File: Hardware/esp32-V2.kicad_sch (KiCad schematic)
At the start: 9 parts, among them J11 PM254-1-17-Z-8.5, J13 Conn_01x08, SW4 SW_Push, SW5 SW_Push, U1 ESP32-S31-WROOM-3-N16R16V

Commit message: S31 fully connected
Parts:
- added TP1, TP3, TP4, TP5: TestPoint, TestPoint:TestPoint_Pad_D1.0mm, symbol YV-library:TestPoint
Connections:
- net I34 is gone; now on net IO37: J11.11 (Pin_11)
- net I35 is gone; now on net IO58-UART0-TX: J11.13 (Pin_13)
- net IO0(boot) is gone; now on net IO45: J11.6 (Pin_6)
- net IO21 is gone; now on net IO35: J11.10 (Pin_10)
- net IO22 is gone; now on net IO43: J11.8 (Pin_8)
- net IO25 is gone; now on net IO47: J11.4 (Pin_4)
- net IO26 is gone; now on net IO48: J11.3 (Pin_3)
- net IO27 is gone; now on net IO46: J11.5 (Pin_5)
- net IO32 is gone; now on net IO44: J11.7 (Pin_7)
- net Vbatt-VN is gone; now on net IO59-UART0-RX: J11.12 (Pin_12)
- net CS: now also U1.60 (GPIO50/ADC2_CH0_N)
- net RST: now also U1.59 (GPIO49/ADC1_CH3_P)
- net SCL: now also U1.62 (GPIO52/ADC2_CH1_N)
- net SD0: now also U1.63 (GPIO53/ADC2_CH1_P)
- net SDA: now also U1.61 (GPIO51/ADC2_CH0_P)
- net at U1.40 (USB_DP): now also TP3.1
- net at U1.41 (USB_DM): now also TP4.1
- net IO35: now reaches U1.44 (GPIO35)
- net at U1.45 (GPIO36*): now also TP1.1
- net IO37: now reaches U1.46 (GPIO37)
- net IO43: now reaches U1.53 (GPIO43/ADC1_CH0_P)
- net IO44: now reaches U1.54 (GPIO44/ADC1_CH1_N)
- net IO45: now reaches U1.55 (GPIO45/ADC1_CH1_P)
- net IO46: now reaches U1.56 (GPIO46/ADC1_CH2_N)
- net IO47: now reaches U1.57 (GPIO47/ADC1_CH2_P)
- net IO48: now reaches U1.58 (GPIO48/ADC1_CH3_N)
- net IO58-UART0-TX: now reaches U1.68 (UART0_TXD/GPIO58)
- net IO59-UART0-RX: now reaches U1.69 (UART0_RXD/GPIO59)
- net at U1.70 (GPIO60): now also TP5.1
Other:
- note removed: "I2S_BCLK"
- note removed: "I2S_DOUT"
- note removed: "I2S_LRC"
- note removed: "SCL"
- note removed: "SDA"

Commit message: Schematic Done
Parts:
- removed TP5: TestPoint, TestPoint:TestPoint_Pad_D1.0mm, symbol YV-library:TestPoint
- added R13, R14: 100k, Resistor_SMD:R_0402_1005Metric, symbol Device:R
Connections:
- net +3.3V: now also R13.1, R14.1
- net BOOT: now also R8.2
- net DE: now also U1.49 (GPIO38); no longer U1.25 (GPIO19)
- net DS0: now also U1.10 (GPIO4); no longer U1.6 (GPIO2)
- net DS1: now also U1.11 (GPIO5); no longer U1.7 (GPIO3)
- net DS10: now also U1.17 (GPIO11); no longer U1.13 (GPIO7)
- net DS11: now also U1.18 (GPIO12); no longer U1.14 (GPIO8)
- net DS12: now also U1.19 (GPIO13); no longer U1.15 (GPIO9)
- net DS13: now also U1.20 (GPIO14); no longer U1.16 (GPIO10)
- net DS16: now also U1.21 (GPIO15); no longer U1.17 (GPIO11)
- net DS17: now also U1.22 (GPIO16); no longer U1.18 (GPIO12)
- net DS18: now also U1.23 (GPIO17); no longer U1.19 (GPIO13)
- net DS19: now also U1.24 (GPIO18); no longer U1.20 (GPIO14)
- net DS2: now also U1.12 (GPIO6); no longer U1.8 (GPIO0/XTAL_32K_N)
- net DS20: now also U1.25 (GPIO19); no longer U1.21 (GPIO15)
- net DS3: now also U1.13 (GPIO7); no longer U1.9 (GPIO1/XTAL_32K_P)
- net DS4: now also U1.14 (GPIO8); no longer U1.10 (GPIO4)
- net DS8: now also U1.15 (GPIO9); no longer U1.11 (GPIO5)
- net DS9: now also U1.16 (GPIO10); no longer U1.12 (GPIO6)
- net EN: now also R14.2; no longer R8.2
- net HS: now also U1.51 (GPIO40); no longer U1.23 (GPIO17)
- net I2C1-SCL: now also U1.9 (GPIO1/XTAL_32K_P); no longer U1.49 (GPIO38)
- net I2C1-SDA: now also U1.8 (GPIO0/XTAL_32K_N); no longer U1.50 (GPIO39)
- net IO43: now also J11.3 (Pin_3); no longer J11.8 (Pin_8)
- net IO44: now also J11.4 (Pin_4); no longer J11.7 (Pin_7)
- net IO45: now also J11.5 (Pin_5); no longer J11.6 (Pin_6)
- net IO46: now also J11.6 (Pin_6); no longer J11.5 (Pin_5)
- net IO47: now also J11.7 (Pin_7); no longer J11.4 (Pin_4)
- net IO48: now also J11.8 (Pin_8); no longer J11.3 (Pin_3)
- net IO58-UART0-TX: now also J11.12 (Pin_12); no longer J11.13 (Pin_13)
- net IO59-UART0-RX: now also J11.13 (Pin_13); no longer J11.12 (Pin_12)
- net PCLK: now also U1.52 (GPIO42/ADC1_CH0_N); no longer U1.22 (GPIO16)
- net Touch-INT: now also U1.7 (GPIO3); no longer U1.51 (GPIO40)
- net Touch-RST: now also U1.6 (GPIO2); no longer U1.52 (GPIO42/ADC1_CH0_N)
- net VS: now also U1.50 (GPIO39); no longer U1.24 (GPIO18)
- net BACKLIGHTen: now reaches U1.70 (GPIO60)
- net BACKLIGHTen: now also R13.2
- no-connect marks 10 -> 8
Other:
- note added: "Cristal needed for RTC Wont use it"
- company: (none) -> Motion Composites
- title: ESP32-Power -> Strain Gauge Data Logger
- moved on the sheet: C29, C31, C32, J11, J13, SW4, SW5, TP1, TP3, TP4, U1

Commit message: Layout: unrouted = 0
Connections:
- no-connect marks 8 -> 0
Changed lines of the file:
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@@
 	)
 	(junction
+		(at 92.71 104.14)
+		(diameter 0)
+		(color 0 0 0 0)
+	)
+	(junction
 		(at 259.08 121.92)
 		(diameter 0)
@@
 	)
 	(junction
+		(at 92.71 106.68)
+		(diameter 0)
+		(color 0 0 0 0)
+	)
+	(junction
+		(at 92.71 109.22)
+		(diameter 0)
+		(color 0 0 0 0)
+	)
+	(junction
 		(at 199.39 24.13)
 		(diameter 0)
@@
 	)
 	(junction
+		(at 92.71 116.84)
+		(diameter 0)
+		(color 0 0 0 0)
+	)
+	(junction
 		(at 39.37 187.96)
 		(diameter 0)
@@
 	)
 	(junction
+		(at 92.71 114.3)
+		(diameter 0)
+		(color 0 0 0 0)
+	)
+	(junction
 		(at 102.87 40.64)
 		(diameter 0)
@@
 	)
 	(junction
-		(at 81.28 22.86)
+		(at 92.71 101.6)
 		(diameter 0)
 		(color 0 0 0 0)
 	)
-	(no_connect
-		(at 73.66 109.22)
-	)
-	(no_connect
-		(at 73.66 111.76)
-	)
-	(no_connect
-		(at 73.66 106.68)
-	)
-	(no_connect
-		(at 73.66 114.3)
-	)
-	(no_connect
-		(at 73.66 104.14)
-	)
-	(no_connect
-		(at 73.66 99.06)
-	)
-	(no_connect
-		(at 73.66 101.6)
+	(junction
+		(at 92.71 111.76)
+		(diameter 0)
+		(color 0 0 0 0)
 	)
-	(no_connect
-		(at 73.66 116.84)
+	(junction
+		(at 81.28 22.86)
+		(diameter 0)
+		(color 0 0 0 0)
 	)
 	(bus_entry
@@
 	(wire
 		(pts
+			(xy 92.71 106.68) (xy 92.71 109.22)
+		)
+		(stroke
+			(width 0)
+			(type default)
+		)
+	)
+	(wire
+		(pts
 			(xy 102.87 30.48) (xy 107.95 30.48)
 		)
@@
 	(wire
 		(pts
-			(xy 71.12 116.84) (xy 73.66 116.84)
+			(xy 71.12 116.84) (xy 92.71 116.84)
+		)
+		(stroke
+			(width 0)
+			(type default)
+		)
+	)
+	(wire
+		(pts
+			(xy 92.71 114.3) (xy 92.71 116.84)
 		)
 		(stroke
@@
 	(wire
 		(pts
-			(xy 71.12 106.68) (xy 73.66 106.68)
+			(xy 71.12 106.68) (xy 92.71 106.68)
 		)
 		(stroke
@@
 	(wire
 		(pts
-			(xy 71.12 111.76) (xy 73.66 111.76)
+			(xy 71.12 111.76) (xy 92.71 111.76)
 		)
 		(stroke
@@
 	(wire
 		(pts
+			(xy 92.71 111.76) (xy 92.71 114.3)
+		)
+		(stroke
+			(width 0)
+			(type default)
+		)
+	)
+	(wire
+		(pts
 			(xy 135.89 110.49) (xy 135.89 123.19)
 		)
@@
 	(wire
 		(pts
+			(xy 92.71 109.22) (xy 92.71 111.76)
+		)
+		(stroke
+			(width 0)
+			(type default)
+		)
+	)
+	(wire
+		(pts
 			(xy 194.31 73.66) (xy 213.36 73.66)
 		)
@@
 	(wire
 		(pts
+			(xy 92.71 101.6) (xy 92.71 104.14)
+		)
+		(stroke
+			(width 0)
+			(type default)
+		)
+	)
+	(wire
+		(pts
 			(xy 71.12 66.04) (xy 107.95 66.04)
 		)
@@
 	(wire
 		(pts
-			(xy 71.12 104.14) (xy 73.66 104.14)
+			(xy 71.12 104.14) (xy 92.71 104.14)
 		)
 		(stroke
@@
 	(wire
 		(pts
+			(xy 92.71 104.14) (xy 92.71 106.68)
+		)
+		(stroke
+			(width 0)
+			(type default)
+		)
+	)
+	(wire
+		(pts
 			(xy 97.79 172.72) (xy 104.14 172.72)
 		)
@@
 	(wire
 		(pts
+			(xy 92.71 99.06) (xy 92.71 101.6)
+		)
+		(stroke
+			(width 0)
+			(type default)
+		)
+	)
+	(wire
+		(pts
 			(xy 194.31 78.74) (xy 213.36 78.74)
 		)
@@
 	(wire
 		(pts
+			(xy 92.71 116.84) (xy 92.71 118.11)
+		)
+		(stroke
+			(width 0)
+			(type default)
+		)
+	)
+	(wire
+		(pts
 			(xy 71.12 63.5) (xy 107.95 63.5)
 		)
@@
 	(wire
 		(pts
-			(xy 71.12 101.6) (xy 73.66 101.6)
+			(xy 71.12 101.6) (xy 92.71 101.6)
 		)
 		(stroke
@@
 	(wire
 		(pts
-			(xy 71.12 99.06) (xy 73.66 99.06)
+			(xy 71.12 99.06) (xy 92.71 99.06)
 		)
 		(stroke
@@
 	(wire
 		(pts
-			(xy 71.12 109.22) (xy 73.66 109.22)
+			(xy 71.12 109.22) (xy 92.71 109.22)
 		)
 		(stroke
@@
 	(wire
 		(pts
-			(xy 71.12 114.3) (xy 73.66 114.3)
+			(xy 71.12 114.3) (xy 92.71 114.3)
 		)
 		(stroke
@@
 					(unit 1)
 				)
+			)
+		)
+	)
+	(symbol
+		(lib_id "power:GND")
+		(at 92.71 118.11 0)
+		(unit 1)
+		(body_style 1)
+		(exclude_from_sim no)
+		(in_bom yes)
+		(on_board yes)
+		(in_pos_files yes)
+		(dnp no)
+		(fields_autoplaced yes)
+		(property "Reference" "#PWR012"
+			(at 92.71 124.46 0)
+			(hide yes)
+			(show_name no)
+			(do_not_autoplace no)
+			(effects
+				(font
+					(size 1.27 1.27)
+				)
+			)
+		)
+		(property "Value" "GND"
+			(at 92.71 123.19 0)
+			(hide yes)
+			(show_name no)
+			(do_not_autoplace no)
+			(effects
+				(font
+					(size 1.27 1.27)
+				)
+			)
+		)
+		(property "Footprint" ""
+			(at 92.71 118.11 0)
+			(hide yes)
+			(show_name no)
+			(do_not_autoplace no)
+			(effects
+				(font
+					(size 1.27 1.27)
+				)
+			)
+		)
+		(property "Datasheet" ""
+			(at 92.71 118.11 0)
+			(hide yes)
+			(show_name no)
+			(do_not_autoplace no)
+			(effects
+				(font
+					(size 1.27 1.27)
+				)
+			)
+		)
+		(property "Description" "Power symbol creates a global label with name \"GND\" , ground"
+			(at 92.71 118.11 0)
+			(hide yes)
+			(show_name no)
+			(do_not_autoplace no)
+			(effects
+				(font
+					(size 1.27 1.27)
+				)
+			)
+		)
+		(pin "1"
+		)
+		(instances
+			(project "esp32-V2"
+				(path "/cee18f8d-8618-44b5-96f4-3f3967d85a92/70414f53-588f-4a4a-b5a5-2152d4a63cd4"
+					(reference "#PWR012")
+					(unit 1)
+				)

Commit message: Layout cleaned
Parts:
- renumbered C32 to C33, C31 to C34, C29 to C6, J13 to J3, J11 to J5, R13 to R19, R8 to R30, R14 to R5, SW5 to SW2, SW4 to SW3, TP3 to TP1, TP4 to TP2, TP1 to TP3, U1 to U3
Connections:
- net USB-Dn renamed USB_D-
- net USB-Dp renamed USB_D+
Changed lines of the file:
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@@
+		)
+	)
+	(hierarchical_label "USB_D+"
+		(shape bidirectional)
+		(at 152.4 134.62 180)
+		(effects
+			(font
+				(size 1.524 1.524)
+			)
+			(justify right)
 		)
 	)
@@
 		)
 	)
-	(hierarchical_label "USB-Dn"
+	(hierarchical_label "USB_D-"
 		(shape bidirectional)
 		(at 152.4 132.08 180)
@@
 		(shape output)
 		(at 93.98 55.88 180)
-		(effects
-			(font
-				(size 1.524 1.524)
-			)
-			(justify right)
-		)
-	)
-	(hierarchical_label "USB-Dp"
-		(shape bidirectional)
-		(at 152.4 134.62 180)
 		(effects
 			(font
@@
 		(in_pos_files yes)
 		(dnp no)
-		(property "Reference" "J13"
+		(property "Reference" "J3"
 			(at 108.204 167.386 0)
 			(show_name no)
@@
 			(project "esp32-V2"
 				(path "/cee18f8d-8618-44b5-96f4-3f3967d85a92/70414f53-588f-4a4a-b5a5-2152d4a63cd4"
-					(reference "J13")
+					(reference "J3")
 					(unit 1)
 				)
@@
 		(in_pos_files yes)
 		(dnp no)
-		(property "Reference" "SW4"
+		(property "Reference" "SW3"
 			(at 266.7 116.586 0)
 			(show_name no)
@@
 			(project "esp32-V2"
 				(path "/cee18f8d-8618-44b5-96f4-3f3967d85a92/70414f53-588f-4a4a-b5a5-2152d4a63cd4"
-					(reference "SW4")
+					(reference "SW3")
 					(unit 1)
 				)
@@
 		(dnp no)
 		(fields_autoplaced yes)
-		(property "Reference" "U1"
+		(property "Reference" "U3"
 			(at 151.13 21.59 0)
 			(show_name no)
@@
 			(project "esp32-V2"
 				(path "/cee18f8d-8618-44b5-96f4-3f3967d85a92/70414f53-588f-4a4a-b5a5-2152d4a63cd4"
-					(reference "U1")
+					(reference "U3")
 					(unit 1)
 				)
@@
 		(in_pos_files yes)
 		(dnp no)
-		(property "Reference" "R13"
+		(property "Reference" "R19"
 			(at 205.74 27.9399 0)
 			(show_name no)
@@
 			(project "esp32-V2"
 				(path "/cee18f8d-8618-44b5-96f4-3f3967d85a92/70414f53-588f-4a4a-b5a5-2152d4a63cd4"
-					(reference "R13")
+					(reference "R19")
 					(unit 1)
 				)
@@
 		(in_pos_files yes)
 		(dnp no)
-		(property "Reference" "SW5"
+		(property "Reference" "SW2"
 			(at 267.716 143.51 0)
 			(show_name no)
@@
 			(project "esp32-V2"
 				(path "/cee18f8d-8618-44b5-96f4-3f3967d85a92/70414f53-588f-4a4a-b5a5-2152d4a63cd4"
-					(reference "SW5")
+					(reference "SW2")
 					(unit 1)
 				)
@@
 		(in_pos_files yes)
 		(dnp no)
-		(property "Reference" "C32"
+		(property "Reference" "C33"
 			(at 258.064 151.384 0)
 			(show_name no)
@@
 			(project "esp32-V2"
 				(path "/cee18f8d-8618-44b5-96f4-3f3967d85a92/70414f53-588f-4a4a-b5a5-2152d4a63cd4"
-					(reference "C32")
+					(reference "C33")
 					(unit 1)
 				)
@@
 		(in_pos_files yes)
 		(dnp no)
-		(property "Reference" "J11"
+		(property "Reference" "J5"
 			(at 29.464 144.526 0)
 			(show_name no)
@@
 			(project "esp32-V2"
 				(path "/cee18f8d-8618-44b5-96f4-3f3967d85a92/70414f53-588f-4a4a-b5a5-2152d4a63cd4"
-					(reference "J11")
+					(reference "J5")
 					(unit 1)
 				)
@@
 		(in_pos_files yes)
 		(dnp no)
-		(property "Reference" "TP3"
+		(property "Reference" "TP1"
 			(at 151.13 127.508 90)
 			(show_name no)
@@
 			(project "esp32-V2"
 				(path "/cee18f8d-8618-44b5-96f4-3f3967d85a92/70414f53-588f-4a4a-b5a5-2152d4a63cd4"
-					(reference "TP3")
+					(reference "TP1")
 					(unit 1)
 				)
@@
 		(in_pos_files yes)
 		(dnp no)
-		(property "Reference" "TP4"
+		(property "Reference" "TP2"
 			(at 153.67 127.508 90)
 			(show_name no)
@@
 			(project "esp32-V2"
 				(path "/cee18f8d-8618-44b5-96f4-3f3967d85a92/70414f53-588f-4a4a-b5a5-2152d4a63cd4"
-					(reference "TP4")
+					(reference "TP2")
 					(unit 1)
 				)
@@
 		(in_pos_files yes)
 		(dnp no)
-		(property "Reference" "C31"
+		(property "Reference" "C34"
 			(at 260.604 124.714 0)
 			(show_name no)
@@
 			(project "esp32-V2"
 				(path "/cee18f8d-8618-44b5-96f4-3f3967d85a92/70414f53-588f-4a4a-b5a5-2152d4a63cd4"
-					(reference "C31")
+					(reference "C34")
 					(unit 1)
 				)
@@
 		(in_pos_files yes)
 		(dnp no)
-		(property "Reference" "R14"
+		(property "Reference" "R5"
 			(at 97.536 36.83 0)
 			(show_name no)
@@
 			(project "esp32-V2"
 				(path "/cee18f8d-8618-44b5-96f4-3f3967d85a92/70414f53-588f-4a4a-b5a5-2152d4a63cd4"
-					(reference "R14")
+					(reference "R5")
 					(unit 1)
 				)
@@
 		(in_pos_files yes)
 		(dnp no)
-		(property "Reference" "TP1"
+		(property "Reference" "TP3"
 			(at 163.83 127.508 90)
 			(show_name no)
@@
 			(project "esp32-V2"
 				(path "/cee18f8d-8618-44b5-96f4-3f3967d85a92/70414f53-588f-4a4a-b5a5-2152d4a63cd4"
-					(reference "TP1")
+					(reference "TP3")
 					(unit 1)
 				)
@@
 		(in_pos_files yes)
 		(dnp no)
-		(property "Reference" "C29"
+		(property "Reference" "C6"
 			(at 82.804 25.654 0)
 			(show_name no)
@@
 			(project "esp32-V2"
 				(path "/cee18f8d-8618-44b5-96f4-3f3967d85a92/70414f53-588f-4a4a-b5a5-2152d4a63cd4"
-					(reference "C29")
+					(reference "C6")
 					(unit 1)
 				)
@@
 		(in_pos_files yes)
 		(dnp no)
-		(property "Reference" "R8"
+		(property "Reference" "R30"
 			(at 195.326 27.686 0)
 			(show_name no)
@@
 			(project "esp32-V2"
 				(path "/cee18f8d-8618-44b5-96f4-3f3967d85a92/70414f53-588f-4a4a-b5a5-2152d4a63cd4"
-					(reference "R8")
+					(reference "R30")
 					(unit 1)
 				)

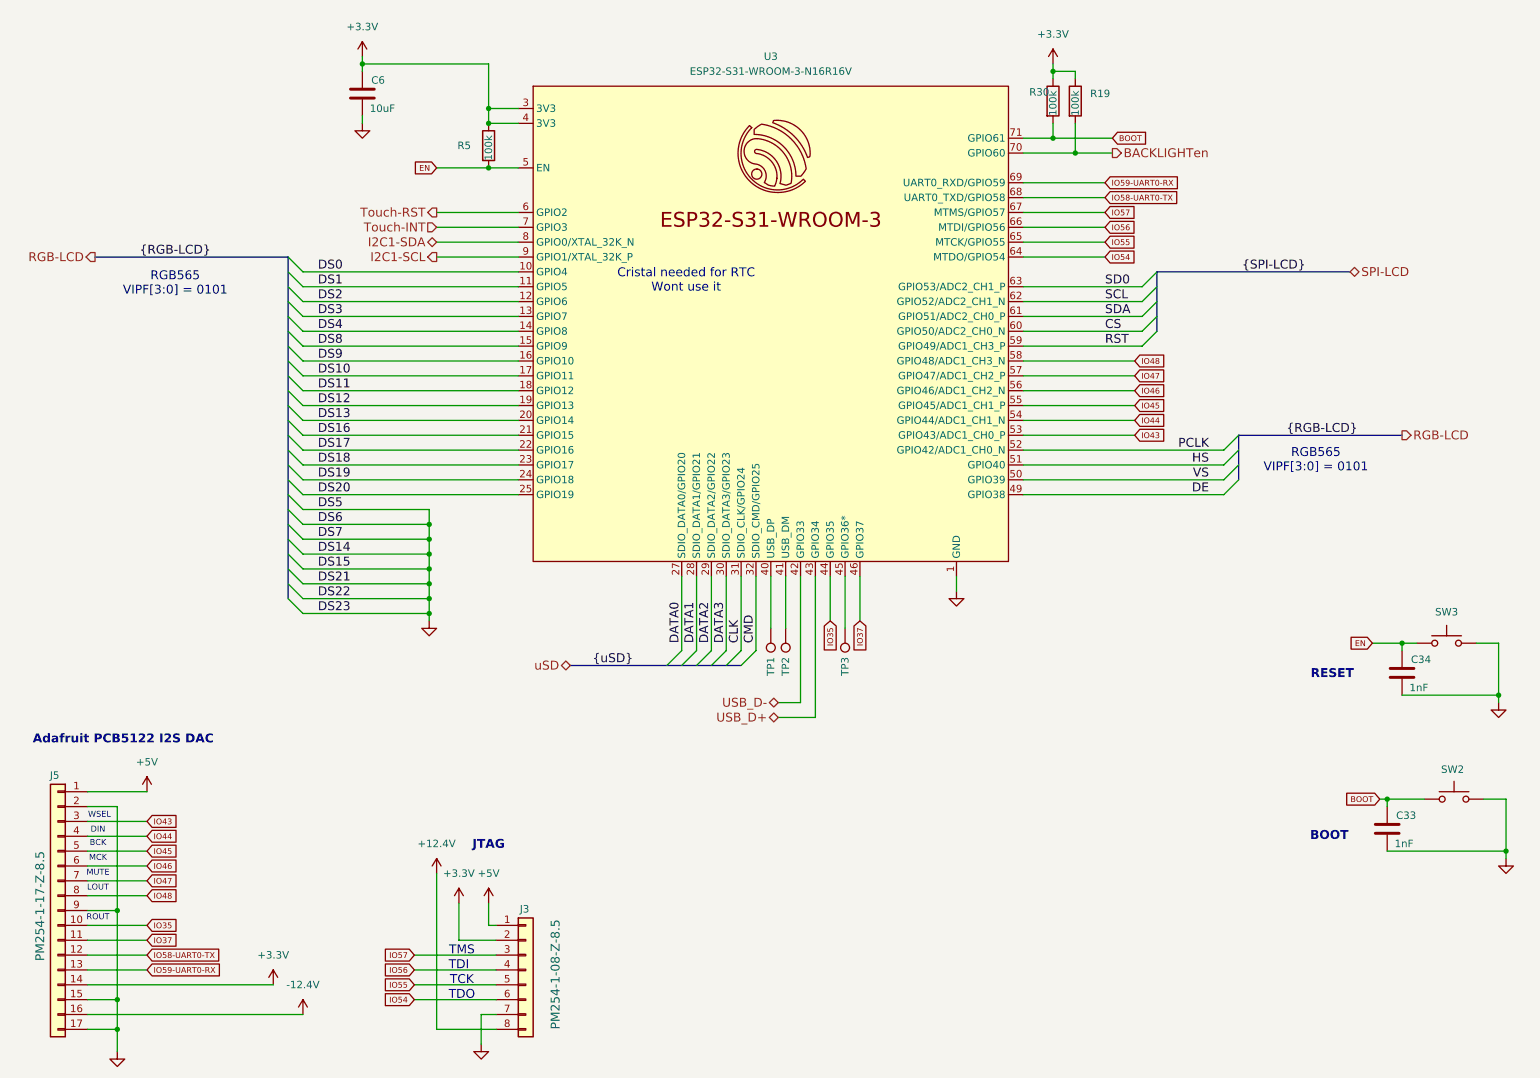
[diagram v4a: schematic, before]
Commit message: Update de la librairy et du BOM
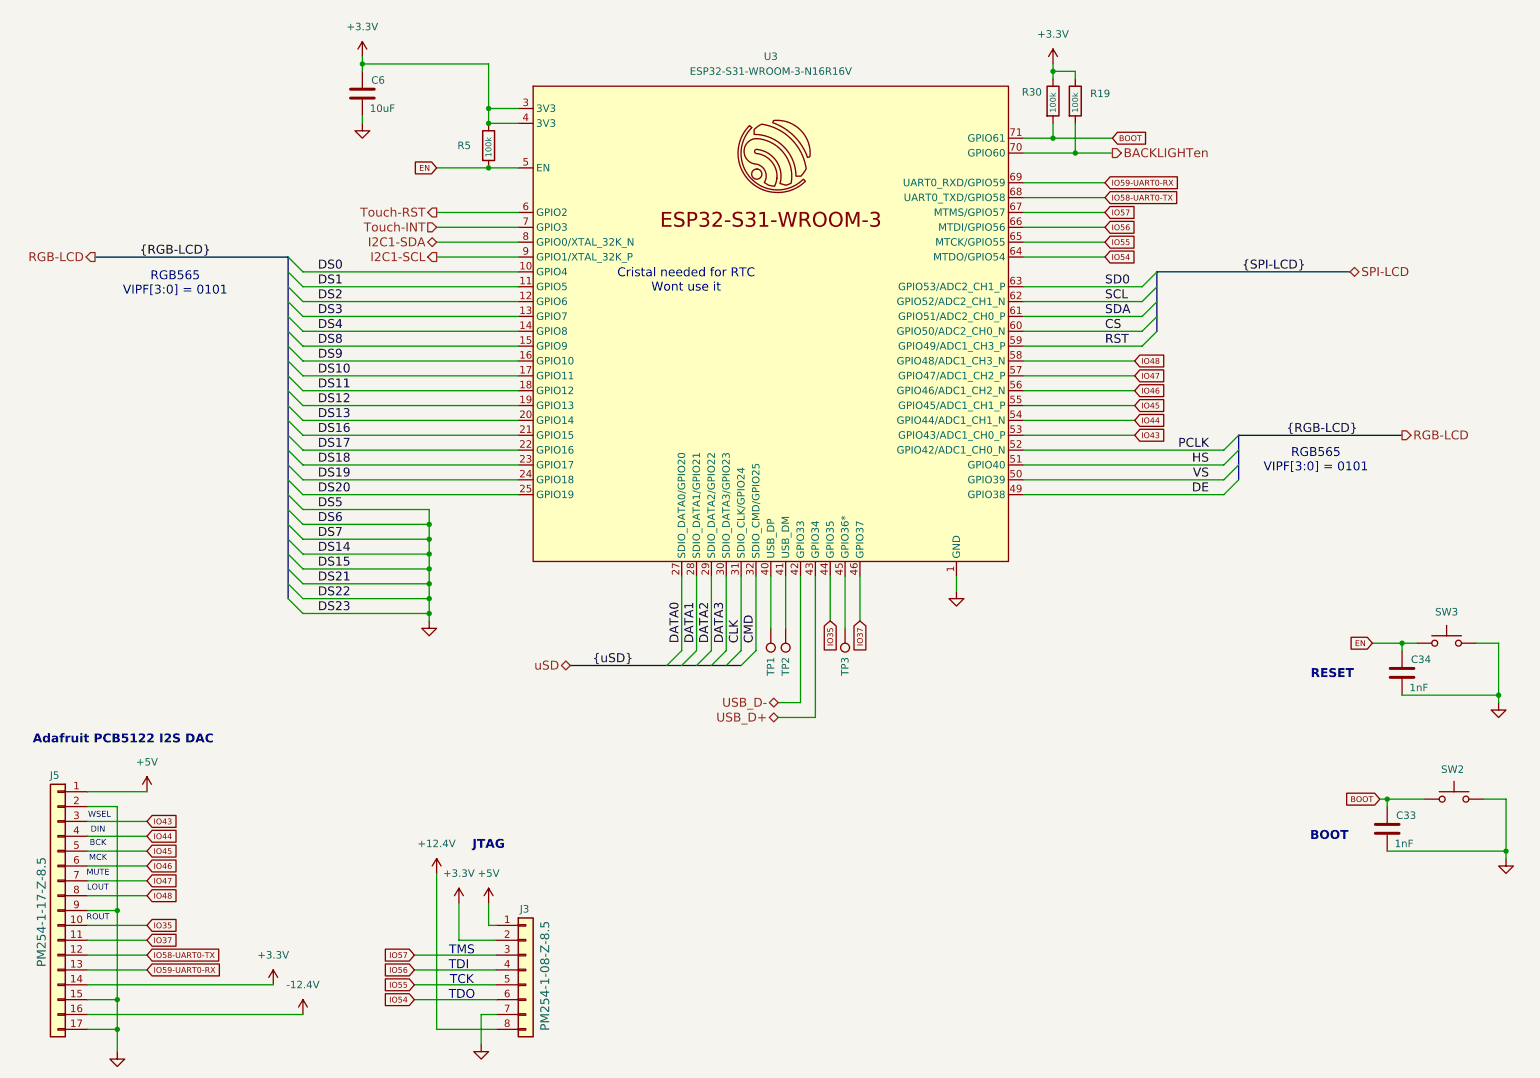
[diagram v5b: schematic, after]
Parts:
- C33, C34: symbol Device:C -> YV-library:CAPN1N00M50V0-00; PartNumber (none) -> GRM1555C1H102GA01D
- C6: symbol Device:C -> YV-library:CAPX10U0M6V30-00; KiLib_Generator SMD_2terminal_chip_molded -> (none); LCSC C20069813 -> C15525; PartNumber (none) -> CL05A106MQ5NUNC
- J3: value Conn_01x08 -> Conn_01x08_F_Header; symbol Connector_Generic:Conn_01x08 -> YV-library:Conn_01x08_F_Header; now in the parts list
- J5: symbol Connector_Generic:Conn_01x17 -> YV-library:Conn_01x17_F_Header; now in the parts list
- R19, R30, R5: symbol Device:R -> YV-library:RES100KM-00; KiLib_Generator SMD_2terminal_chip_molded -> (none); PartNumber (none) -> 0402WGF1003TCE
- SW2, SW3: value SW_Push -> SW-000001; symbol Switch:SW_Push -> YV-library:SW-000001; now in the parts list
- U3: footprint PCM_Espressif:ESP32-S31-WROOM-3 -> YV:ESP32-S31-WROOM-3
